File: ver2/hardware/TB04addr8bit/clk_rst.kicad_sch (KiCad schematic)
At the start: 30 parts, among them SW2 SW_Push, SW4 SW_Push, SW7 SW_Rotary_1x9_MP, U18 74HC14, U19 4060, Y1 32.768KHz

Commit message: ver2: ゲートICをgatesシートへ集約しアノテーションを掛け直し
- 分散していた8パッケージ(U1/U2/U5/U25/U35/U36/U37/U51)をgatesシートへ集約
- シートをまたぐ11本をグローバルラベル化(~P4/~P5/~OUT_SEL/~CS_RAM/
  ~OE_ROM/CLK_C/CLK_Z/PC_CNT_EN/~PC_PE/~Ena_RS01/~Enb_RS01)
- U40のP2入力がROM_SELに吸着していたのを修正(RAM_SELが逆条件だった)
- !P5の重複インバータを解消、未使用ゲート入力7本をGNDへ
- ALU入力MUXをinPut→PC、PCカウンタをaddrMUX→PCへ移動
- 全体を再アノテーション(シート順採番)。旧→新の対応は電気的変化なしを確認

Co-Authored-By: Claude Opus 5 <noreply@anthropic.com>
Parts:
- renumbered C30 to C501, C31 to C502, C32 to C503, C33 to C504, C34 to C505, C35 to C506, D34 to D501, D35 to D502, H1 to H501, H2 to H502, H3 to H503, H4 to H504, R4 to R501, R5 to R502, R6 to R503, R7 to R504, R8 to R505, R9 to R506, R10 to R507, R11 to R508, R17 to R509, R12 to R510, R13 to R511, R14 to R512, SW2 to SW501, SW7 to SW502, SW4 to SW503, U18 to U501, U19 to U502, Y1 to Y501

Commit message: ver2: 掃除とタイミング是正(ROMのEXEゲート・フラグクロックをFCH1へ)
- 消費先ゼロだったU1302(RAM_SEL/STACK_SEL/IN_SEL/P6)を削除し空きゲート入力をGNDへ
- /OE_ROMの条件を生の~WRから~WR_EXE(=!(WR&EXE))へ変更
  書込命令の次のフェッチでROMが閉じる問題を解消
- フラグDFFのクロックゲートをEXEからFCH1へ(CLK_C=FCH1&C_WE)
  INのZが間に合わない件と、Cin=C_prevの帰還でADD/SUBの結果が壊れる件を解消
- いずれもネットリストで接続変化を照合済み。ERCはエラー98(全てwire_dangling)・警告0

Co-Authored-By: Claude Opus 5 <noreply@anthropic.com>
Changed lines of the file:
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@@
 	(wire
 		(pts
-			(xy 372.11 114.3) (xy 379.73 114.3)
+			(xy 372.11 114.3) (xy 378.46 114.3)
 		)
 		(stroke

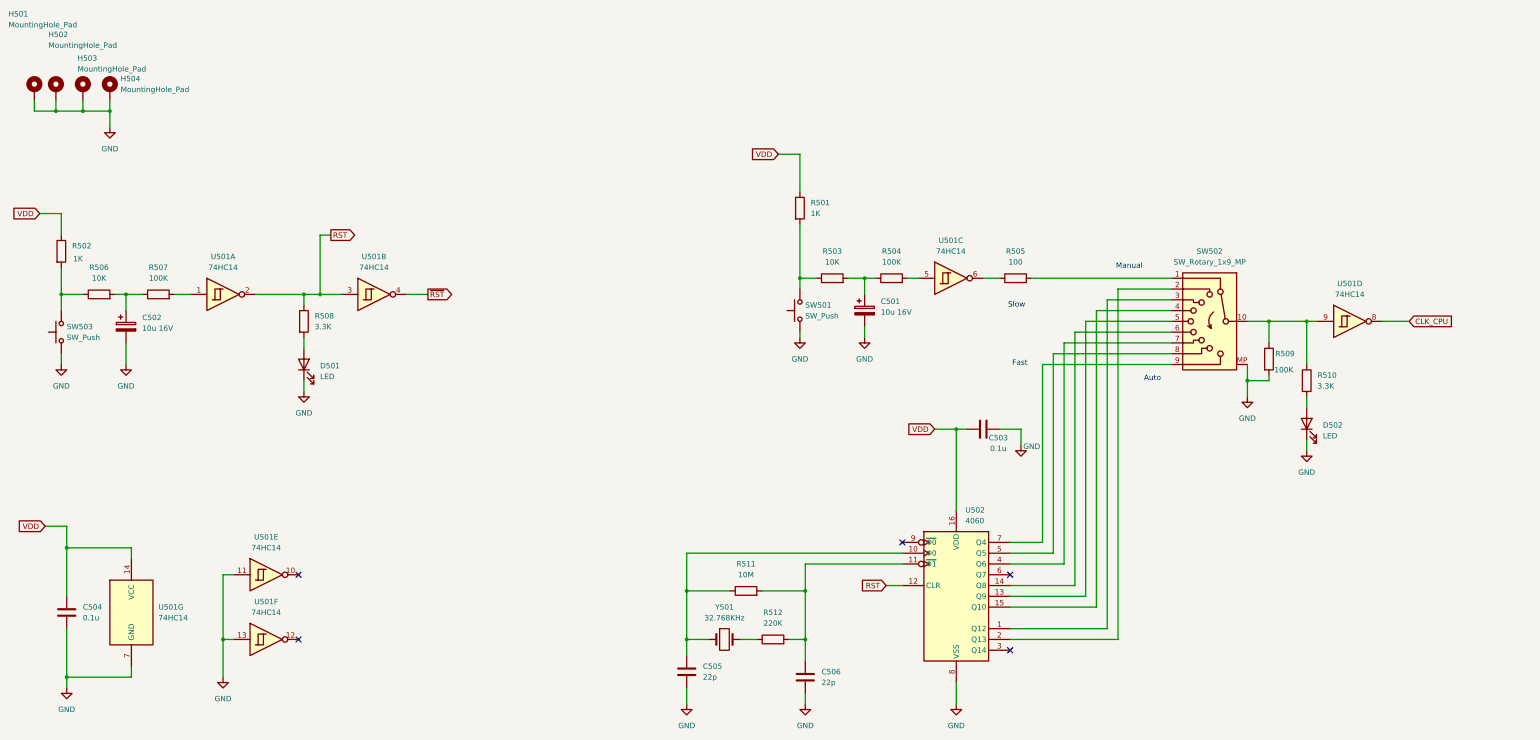
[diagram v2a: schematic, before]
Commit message: ver2: I/Oを4ch化しアドレスバスの浮きを解消(OUTは377化・RAMのCSをEXEゲート)
- I/Oアドレス源244・port位置MUX157・portデコード139を追加し、IN244×4/OUT×4に拡張。
  IN/OUT実行中も 0xF8|port / 0xFC|port をアドレスバスへ出すことで、全相・全命令で
  アドレスバスが必ず1つに駆動される状態にした(OUTのRAM誤書込・INのMD衝突を構造的に解消)。
- OUTポートを74HC273→74HC377へ。~E=139出力・CP=~CLK_CPUとし、クロックゲートなしで
  EXE中間の1回だけ取り込む(取り込み余裕が15ns→半相)。
- ~CS_RAM を !(RAM_STK_SEL & EXE) に変更(CS_RAMノード新設)。EXE末に出る第2の書込パルスを
  約38nsに短縮しtWP未満に収めた。フェッチ3相でRAMが非選択になる副次効果あり。
- OUTコネクタのピン配列を7segIF J1に合わせて入れ替え(D3出力がVDDへ短絡する組合せを回避)。
- パスコンが無かった2シート(outPort・PC_aluMux)に追加。RS.kicad_sch を RS00.kicad_sch へ改名。

Co-Authored-By: Claude Opus 5 <noreply@anthropic.com>
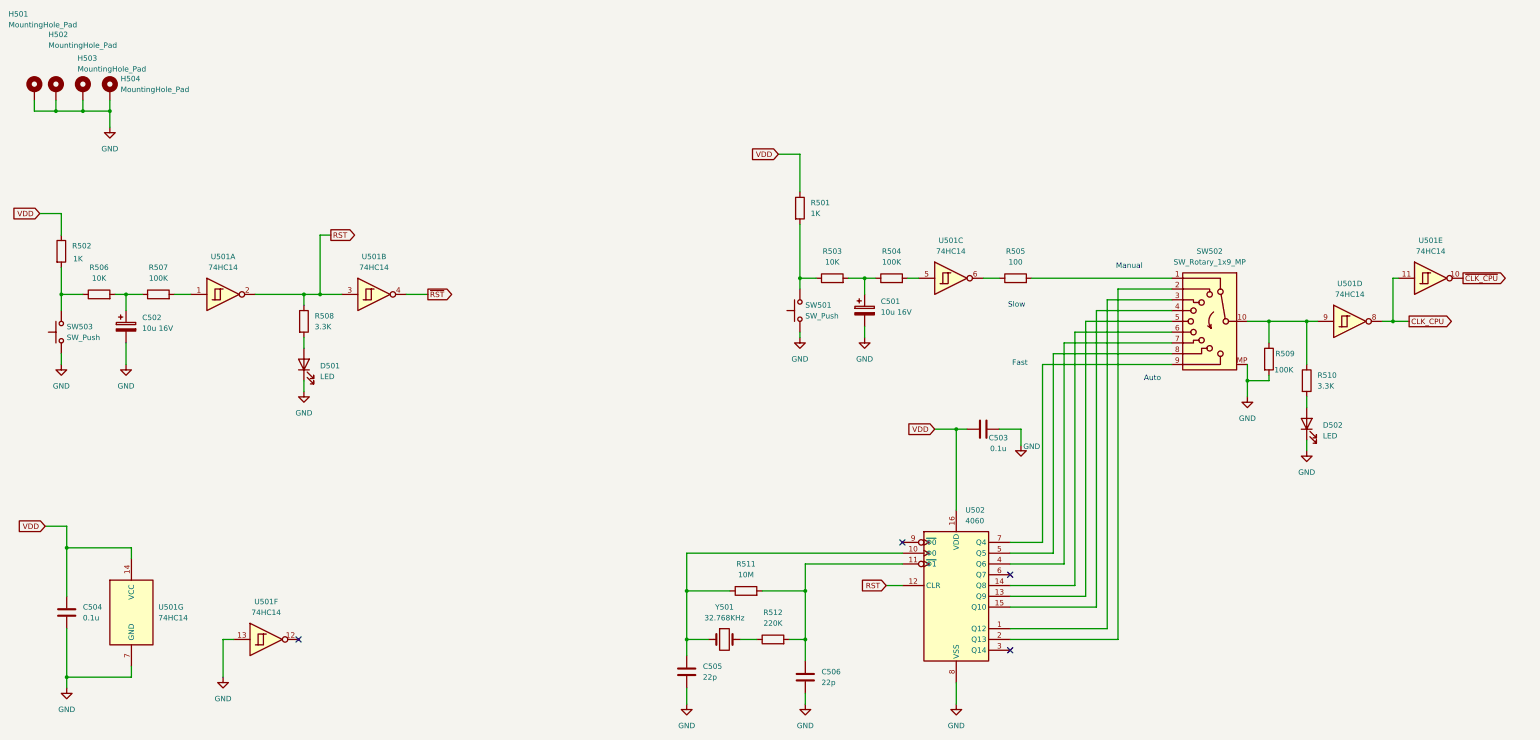
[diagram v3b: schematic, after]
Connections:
- net CLK_CPU: now also U501.11
- net GND: no longer U501.11
- net ~{CLK_CPU}: now reaches U501.10
- no-connect marks 5 -> 4
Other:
- moved on the sheet: U501E
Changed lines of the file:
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@@
 	)
 	(junction
-		(at 99.06 189.23)
-		(diameter 0)
-		(color 0 0 0 0)
-	)
-	(junction
 		(at 62.23 167.64)
 		(diameter 0)
@@
 	)
 	(junction
+		(at 374.65 114.3)
+		(diameter 0)
+		(color 0 0 0 0)
+	)
+	(junction
 		(at 354.33 114.3)
 		(diameter 0)
@@
 	)
 	(no_connect
-		(at 116.84 173.99)
-	)
-	(no_connect
 		(at 259.08 166.37)
 	)
@@
 	(wire
 		(pts
-			(xy 372.11 114.3) (xy 378.46 114.3)
+			(xy 372.11 114.3) (xy 374.65 114.3)
 		)
 		(stroke
@@
 	(wire
 		(pts
+			(xy 374.65 114.3) (xy 378.46 114.3)
+		)
+		(stroke
+			(width 0)
+			(type default)
+		)
+	)
+	(wire
+		(pts
 			(xy 60.96 107.95) (xy 60.96 111.76)
 		)
@@
 	(wire
 		(pts
+			(xy 374.65 104.14) (xy 374.65 114.3)
+		)
+		(stroke
+			(width 0)
+			(type default)
+		)
+	)
+	(wire
+		(pts
 			(xy 234.95 91.44) (xy 234.95 104.14)
 		)
@@
 	(wire
 		(pts
-			(xy 101.6 173.99) (xy 99.06 173.99)
-		)
-		(stroke
-			(width 0)
-			(type default)
-		)
-	)
-	(wire
-		(pts
 			(xy 304.8 181.61) (xy 304.8 111.76)
 		)
@@
 	(wire
 		(pts
-			(xy 99.06 173.99) (xy 99.06 189.23)
+			(xy 226.06 177.8) (xy 236.22 177.8)
 		)
 		(stroke
@@
 	(wire
 		(pts
-			(xy 226.06 177.8) (xy 236.22 177.8)
+			(xy 142.24 107.95) (xy 147.32 107.95)
 		)
 		(stroke
@@
 	(wire
 		(pts
-			(xy 142.24 107.95) (xy 147.32 107.95)
+			(xy 118.11 107.95) (xy 121.92 107.95)
 		)
 		(stroke
@@
 	(wire
 		(pts
-			(xy 118.11 107.95) (xy 121.92 107.95)
+			(xy 289.56 104.14) (xy 322.58 104.14)
 		)
 		(stroke
@@
 	(wire
 		(pts
-			(xy 289.56 104.14) (xy 322.58 104.14)
+			(xy 354.33 114.3) (xy 354.33 124.46)
 		)
 		(stroke
@@
 	(wire
 		(pts
-			(xy 354.33 114.3) (xy 354.33 124.46)
+			(xy 208.28 168.91) (xy 208.28 177.8)
 		)
 		(stroke
@@
 	(wire
 		(pts
-			(xy 208.28 168.91) (xy 208.28 177.8)
+			(xy 375.92 104.14) (xy 374.65 104.14)
 		)
 		(stroke
@@
 	)
 	(global_label "CLK_CPU"
-		(shape input)
+		(shape output)
 		(at 378.46 114.3 0)
 		(fields_autoplaced yes)
@@
 		)
 	)
+	(global_label "~{CLK_CPU}"
+		(shape output)
+		(at 391.16 104.14 0)
+		(fields_autoplaced yes)
+		(effects
+			(font
+				(size 1.27 1.27)
+			)
+			(justify left)
+		)
+		(property "Intersheetrefs" "${INTERSHEET_REFS}"
+			(at 402.5514 104.14 0)
+			(show_name no)
+			(do_not_autoplace no)
+			(effects
+				(font
+					(size 1.27 1.27)
+				)
+				(justify left)
+			)
+		)
+	)
 	(global_label "VDD"
 		(shape input)
@@
 	(symbol
 		(lib_id "74xx:74HC14")
-		(at 109.22 173.99 0)
+		(at 383.54 104.14 0)
 		(unit 5)
 		(body_style 1)
@@
 		(dnp no)
 		(property "Reference" "U501"
-			(at 109.22 165.1 0)
+			(at 383.54 95.25 0)
 			(show_name no)
 			(do_not_autoplace no)
@@
 		)
 		(property "Value" "74HC14"
-			(at 109.22 167.64 0)
+			(at 383.54 97.79 0)
 			(show_name no)
 			(do_not_autoplace no)
@@
 		)
 		(property "Footprint" "Package_DIP:DIP-14_W7.62mm_Socket"
-			(at 109.22 173.99 0)
+			(at 383.54 104.14 0)
 			(hide yes)
 			(show_name no)
@@
 		)
 		(property "Datasheet" "http://www.ti.com/lit/gpn/sn74HC14"
-			(at 109.22 173.99 0)
+			(at 383.54 104.14 0)
 			(hide yes)
 			(show_name no)
@@
 		)
 		(property "Description" "Hex inverter schmitt trigger"
-			(at 109.22 173.99 0)
+			(at 383.54 104.14 0)
 			(hide yes)
 			(show_name no)
